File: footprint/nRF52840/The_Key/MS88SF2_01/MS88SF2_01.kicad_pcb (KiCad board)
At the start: 2 copper layers, 62.2 x 22.6 mm, 3 parts, among them J1 Conn_01x13_Female, J2 Conn_01x14_Female, U1 MS88SF2

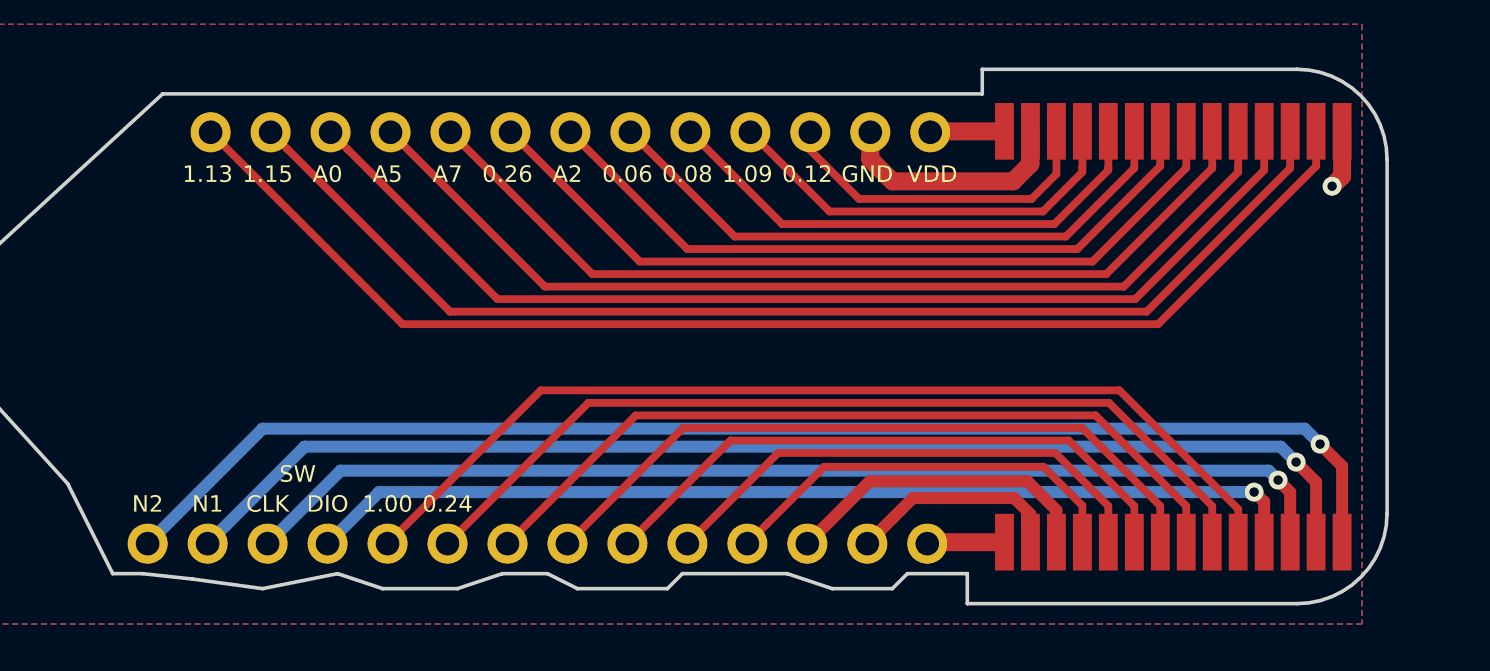
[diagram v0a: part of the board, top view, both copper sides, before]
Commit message: Add MS88SF2
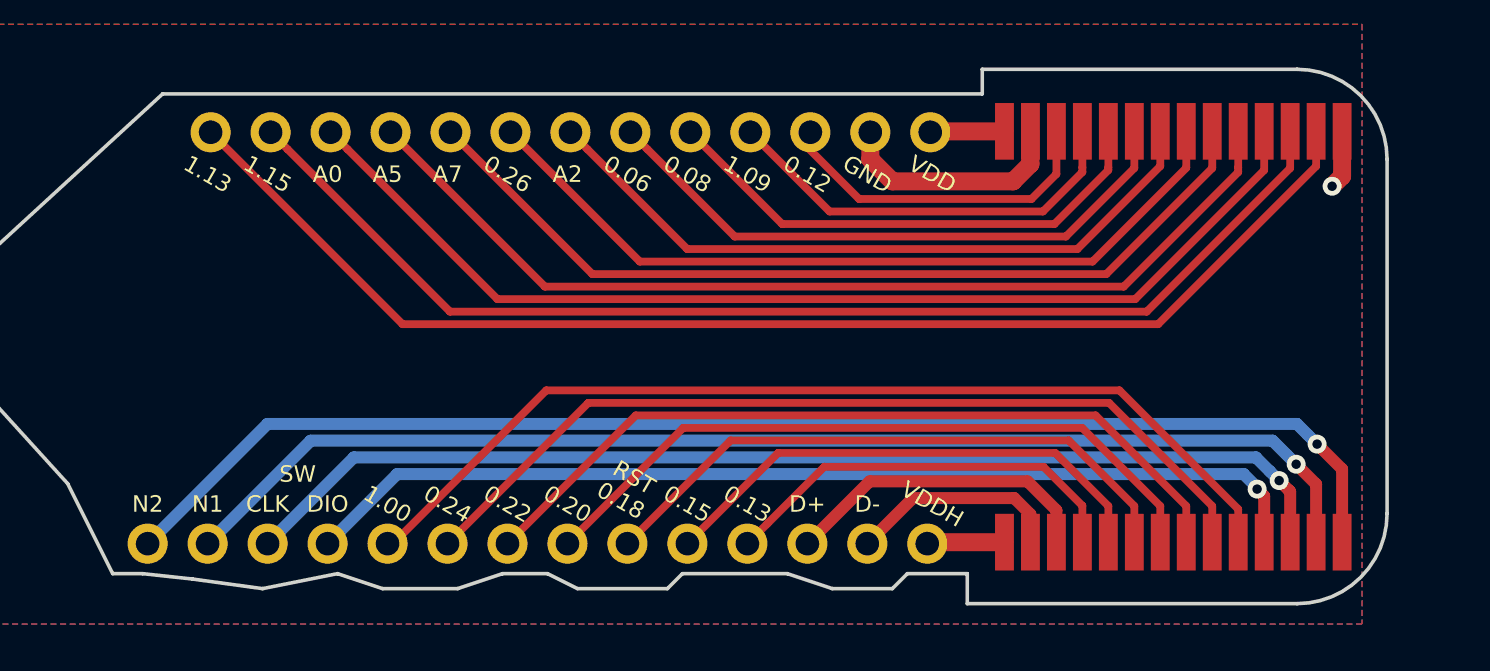
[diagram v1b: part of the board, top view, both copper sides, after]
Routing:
- net /SWDIO: track 42.5 -> 43.3 mm
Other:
- board text added: "0.13"
- board text added: "0.15"
- board text added: "0.20"
- board text added: "0.22"
- board text added: "D+"
- board text added: "D-"
- board text added: "RST 0.18"
- board text added: "VDDH"
